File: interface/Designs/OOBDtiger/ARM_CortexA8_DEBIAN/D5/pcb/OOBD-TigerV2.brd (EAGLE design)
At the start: 63.4 x 38.2 mm, 65 parts, among them U1 SY6280, U10 MP1482DS, U2 SN65HVD230(SO8), U6 SN65HVD230(SO8)

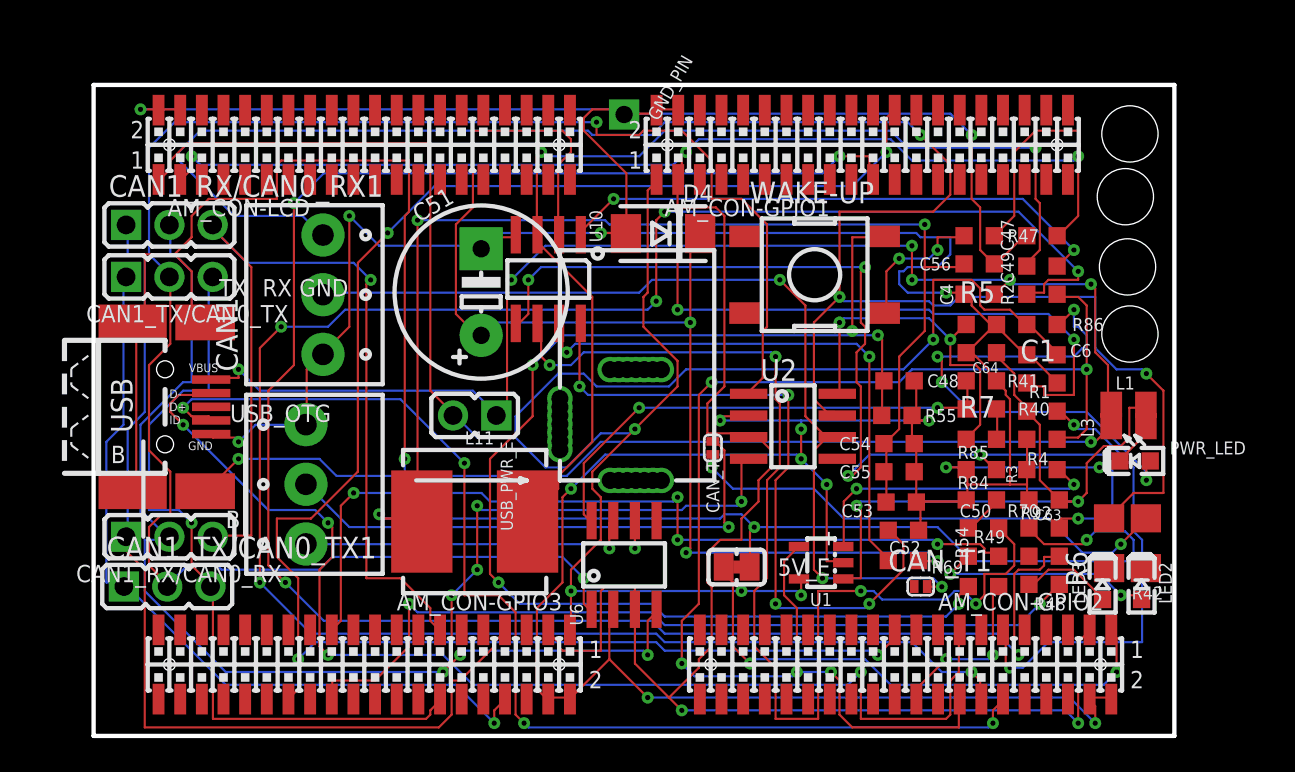
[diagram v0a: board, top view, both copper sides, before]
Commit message: Verzeichnis enhaelt jetzt noch die Schematics & PCB von Audiocape und die aktualisierten Dateien von OOBD-Tiger V2. Im Moment in das falsche IC TLV320AIC3104. Housing und Package vom TLV320AIC3107 müssen noch erzeugt werden, lib dazu habe ich nicht fertig gefunden. Werde das 04 als Vorlage nehmen.
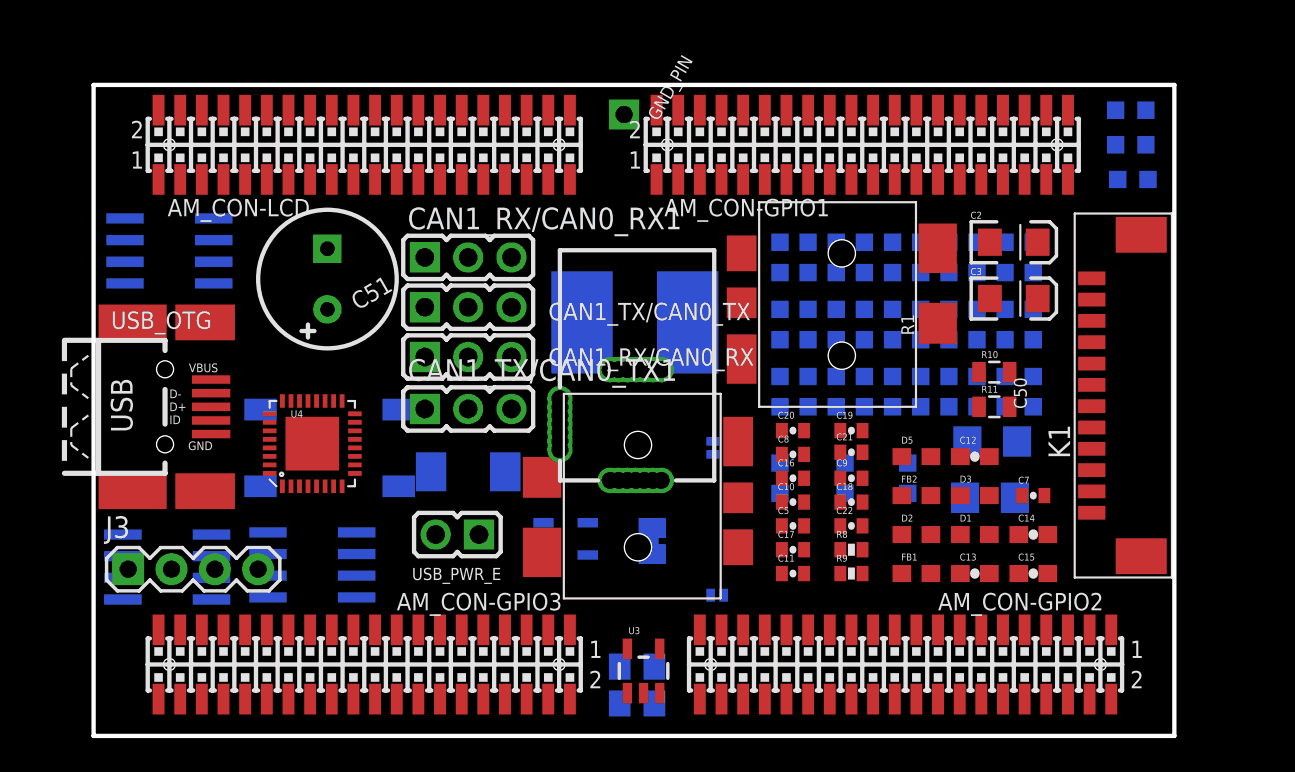
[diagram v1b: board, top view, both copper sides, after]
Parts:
- removed CAN, CAN1: TB3-3.5mm, DOUBLE-SIDE:CON3/3.5MM
- removed FID1, FID2, FID3: FIDUCIAL, SparkFunEagle-6-6-07:FIDUCIAL-1X3
- added C10, C11, C16, C17, C8, C9: 0.1uf, SparkFun-Passives:0402-CAP
- added C12, C13, C14, C15: 10uf,10V, SparkFun-Passives:0603-CAP
- added C18, C19, C5, C7: 47pF, SparkFun-Passives:0402-CAP
- added C2, C3: 47uf, SparkFun-Capacitors:EIA3216
- added C20: 1uf, SparkFun-Passives:0402-CAP
- added C21: .01uf, SparkFun-Passives:0402-CAP
- added C22: 2.2uf, SparkFun-Passives:0402-CAP
- added D1, D2, D3, D5: PGB0010603MR, CircuitCo:0603
- added FB1, FB2: FB, SparkFun-Passives:0603
- added J2, U$3: SJ1-3515-SMT-TR, audio-jack:JACK-SMT
- added J3: (no value), SparkFun-Connectors:1X04
- added K1: 653112124022, EagleLibrary_Wuerth_Elektronik _eiCan_Wire_to_Board_Connectors_v6_20150113:653112124022
- added R10, R11: 0, SparkFun-Passives:0805
- added R8, R9: 33, SparkFun-Passives:0402-RES
- added U3: V_REG_LDOSMD, SparkFun-PowerIC:SOT23-5
- added U4: TLV320AIC3104, CircuitCo:QFN-32
- C51: device rcl:E5-10,5 -> rcl:E3,5-8
- moved L3 33.1 mm to (31.9, 1.91), flipped to the bottom
- moved L1 32.7 mm to (31.9, 4.06), flipped to the bottom
- moved U6 32.4 mm to (4.45, 28.4), flipped to the bottom, turned to 270 degrees
- moved WAKE-UP 30.2 mm to (13.8, 16.9), flipped to the bottom
- moved U2 29.3 mm to (12.8, 10.0), flipped to the bottom
- moved U10 28.0 mm to (4.32, 9.91), flipped to the bottom, turned to 270 degrees
- moved LED2 27.8 mm to (60.8, 36.7), flipped to the bottom, turned to 0 degrees
- moved LED3 25.8 mm to (60.8, 34.7), flipped to the bottom, turned to 0 degrees
- moved CAN1_TX/CAN0_TX1 20.5 mm to (22.0, 19.2)
- moved CAN1_RX/CAN0_RX 20.5 mm to (22.0, 22.2)
- moved R54 19.3 mm to (53.5, 28.1), flipped to the bottom, turned to 270 degrees
- moved R48 19.2 mm to (55.1, 28.1), flipped to the bottom, turned to 270 degrees
- moved D4 18.1 mm to (22.0, 15.5), flipped to the bottom
- moved R92 18.0 mm to (51.8, 28.1), flipped to the bottom, turned to 90 degrees
- moved CAN1_RX/CAN0_RX1 17.6 mm to (22.0, 28.1)
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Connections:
- new net 1.8V: C11.1, C15.2, C22.1, U3.5, U4.32
- new net 3.3V: C10.1, C14.2, C20.1, FB2.2, U3.1, U3.3, U4.7
- new net AGND: C12.1, C13.1, C18.2, C19.1, C5.2, C7.2, C8.2, C9.2, D1.1, D2.1, D3.1, D5.1, FB1.1, J2.1, U$3.1, U4.17, U4.26
- new net AUD_3V3: C12.2, C13.2, C8.1, C9.1, FB2.1, U4.18, U4.24, U4.25
- new net AUD_BCLK: U4.2
- new net AUD_DIN: U4.5
- new net AUD_DOUT: U4.4
- new net AUD_HPLOUT: C2.A, R10.2, U4.19
- new net AUD_HPROUT: C3.A, R11.2, U4.23
- new net AUD_MCLK: U4.1
- new net AUD_WCLK: U4.3
- new net DGND: C10.2, C11.2, C14.1, C15.1, C20.2, C21.2, C22.2, FB1.2, U3.2, U4.21, U4.6, U4.EP
- new net J1: C7.1, D2.2, R8.1, U$3.2
- new net LEFT_LOM: J3.1, U4.28
- new net LEFT_LOP: J3.2, U4.27
- new net LINE1LP: C16.2, U4.14
- new net LINE1RP: C17.1, U4.16
- new net N$10: C2.C, R10.1, R8.2
- new net N$14: C3.C, R11.1, R9.2
- new net N$15: C5.1, D1.2, R9.1, U$3.3
- new net N$16: C17.2, C19.2, D3.2, J2.3
- new net N$17: C16.1, C18.1, D5.2, J2.2
- new net N$18: C21.1, U3.4
- new net RESETN: U4.31
- new net RIGHT_LOP: J3.4, U4.29
- new net RIGHT_ROM: J3.3, U4.30
- new net SCL: U4.8
- new net SDA: U4.9
- net CANH: now also K1.5; no longer CAN.3
- net CANH1: now also K1.1; no longer CAN1.3
- net CANL: now also K1.7; no longer CAN.2
- net CANL1: now also K1.3; no longer CAN1.2
- net GND: now also K1.4; no longer CAN.1, CAN1.1
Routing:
- net GND: track 295.3 -> 0.00 mm, vias 16 -> 0
- net VCC: track 196.9 -> 0.00 mm, vias 7 -> 0
- net +5V: track 165.4 -> 0.00 mm, vias 7 -> 0
- net N$12: track 127.1 -> 0.00 mm, vias 5 -> 0
- net USB0_CE: track 119.2 -> 0.00 mm, vias 6 -> 0
- net CANH1: track 113.3 -> 0.00 mm, vias 3 -> 0
- net N$266: track 113.0 -> 0.00 mm, vias 3 -> 0
- net N$13: track 112.6 -> 0.00 mm, vias 4 -> 0
- net CAN_TX: track 108.2 -> 0.00 mm, vias 2 -> 0
- net SYS_RESETN: track 102.5 -> 0.00 mm, vias 4 -> 0
- net CAN_RX: track 89.4 -> 0.00 mm, vias 7 -> 0
- net USB0-DRV: track 79.6 -> 0.00 mm, vias 5 -> 0
- net N$44: track 76.9 -> 0.00 mm, vias 5 -> 0
- net N$3: track 72.7 -> 0.00 mm, vias 3 -> 0
- net +5V_OTG_PWR: track 72.5 -> 0.00 mm, vias 6 -> 0
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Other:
- board text removed: "B"
